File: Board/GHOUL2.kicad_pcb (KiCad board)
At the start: 2 copper layers, 105.4 x 88.9 mm, 29 parts

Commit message: fixed jb's poor job
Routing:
- net SDA: track 81.5 -> 83.0 mm
- net SCL: track 66.0 -> 67.5 mm
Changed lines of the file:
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@@
     (effects (font (size 1 1) (thickness 0.15)))
   )
+  (segment (start 118.063827 71.062) (end 146.259251 71.062) (width 0.25) (layer "F.Cu") (net 1))
+  (segment (start 151.384 76.2) (end 152.720991 76.2) (width 0.25) (layer "F.Cu") (net 1))
+  (segment (start 146.259251 71.062) (end 151.384 76.186749) (width 0.25) (layer "F.Cu") (net 1))
+  (segment (start 151.384 76.186749) (end 151.384 76.2) (width 0.25) (layer "F.Cu") (net 1))
+  (segment (start 152.720991 76.2) (end 153.67 77.149009) (width 0.25) (layer "F.Cu") (net 1))
+  (segment (start 113.941827 75.184) (end 118.063827 71.062) (width 0.25) (layer "F.Cu") (net 1))
+  (segment (start 103.632 73.66) (end 105.156 75.184) (width 0.25) (layer "F.Cu") (net 1))
+  (segment (start 153.67 77.149009) (end 153.67 81.28) (width 0.25) (layer "F.Cu") (net 1))
   (segment (start 153.67 81.28) (end 152.4 82.55) (width 0.25) (layer "F.Cu") (net 1))
-  (segment (start 113.941827 75.184) (end 118.063827 71.062) (width 0.25) (layer "F.Cu") (net 1))
-  (segment (start 153.67 77.149009) (end 153.67 81.28) (width 0.25) (layer "F.Cu") (net 1))
-  (segment (start 151.275 76.077749) (end 152.59874 76.077749) (width 0.25) (layer "F.Cu") (net 1))
-  (segment (start 152.59874 76.077749) (end 153.67 77.149009) (width 0.25) (layer "F.Cu") (net 1))
-  (segment (start 118.063827 71.062) (end 146.259251 71.062) (width 0.25) (layer "F.Cu") (net 1))
-  (segment (start 146.259251 71.062) (end 151.275 76.077749) (width 0.25) (layer "F.Cu") (net 1))
   (segment (start 105.156 75.184) (end 113.941827 75.184) (width 0.25) (layer "F.Cu") (net 1))
-  (segment (start 103.632 73.66) (end 105.156 75.184) (width 0.25) (layer "F.Cu") (net 1))
   (segment (start 187.065 113.03) (end 192.024 113.03) (width 0.25) (layer "F.Cu") (net 2))
   (segment (start 171.965 130.055) (end 185.47 130.055) (width 0.25) (layer "F.Cu") (net 3))
@@
   (segment (start 148.810405 90.075) (end 145.955 90.075) (width 0.25) (layer "F.Cu") (net 22))
   (segment (start 123.952 73.66) (end 140.367 90.075) (width 0.25) (layer "F.Cu") (net 22))
-  (segment (start 152.720991 121.92) (end 131.025 121.92) (width 0.25) (layer "F.Cu") (net 23))
+  (segment (start 152.720991 121.92) (end 131.064 121.92) (width 0.25) (layer "F.Cu") (net 23))
   (segment (start 152.4 125.73) (end 153.525 124.605) (width 0.25) (layer "F.Cu") (net 23))
+  (segment (start 127.349 118.205) (end 127.31 118.205) (width 0.25) (layer "F.Cu") (net 23))
   (segment (start 153.525 122.724009) (end 152.720991 121.92) (width 0.25) (layer "F.Cu") (net 23))
   (segment (start 153.525 124.605) (end 153.525 122.724009) (width 0.25) (layer "F.Cu") (net 23))
-  (segment (start 131.025 121.92) (end 127.31 118.205) (width 0.25) (layer "F.Cu") (net 23))
-  (segment (start 127.31 120.745) (end 129.755 123.19) (width 0.25) (layer "F.Cu") (net 24))
-  (segment (start 129.755 123.19) (end 152.4 123.19) (width 0.25) (layer "F.Cu") (net 24))
-  (segment (start 155.822591 90.17) (end 154.94 90.17) (width 0.25) (layer "F.Cu") (net 25))
+  (segment (start 131.064 121.92) (end 127.349 118.205) (width 0.25) (layer "F.Cu") (net 23))
+  (segment (start 127.31 120.745) (end 128.935 122.37) (width 0.25) (layer "F.Cu") (net 24))
+  (segment (start 128.935 122.37) (end 151.58 122.37) (width 0.25) (layer "F.Cu") (net 24))
+  (segment (start 151.58 122.37) (end 152.4 123.19) (width 0.25) (layer "F.Cu") (net 24))
+  (segment (start 151.035 111.76) (end 145.955 106.68) (width 0.25) (layer "F.Cu") (net 25))
+  (segment (start 167.64 92.71) (end 167.64 93.472) (width 0.25) (layer "F.Cu") (net 25))
+  (segment (start 167.64 92.71) (end 166.82 91.89) (width 0.25) (layer "F.Cu") (net 25))
   (segment (start 147.042 78.462) (end 145.955 77.375) (width 0.25) (layer "F.Cu") (net 25))
-  (segment (start 152.941496 111.76) (end 151.035 111.76) (width 0.25) (layer "F.Cu") (net 25))
-  (segment (start 167.64 92.71) (end 163.83 96.52) (width 0.25) (layer "F.Cu") (net 25))
-  (segment (start 154.94 90.17) (end 153.525 88.755) (width 0.25) (layer "F.Cu") (net 25))
-  (segment (start 153.525 88.755) (end 150.985 88.755) (width 0.25) (layer "F.Cu") (net 25))
-  (segment (start 167.64 92.71) (end 158.362591 92.71) (width 0.25) (layer "F.Cu") (net 25))
-  (segment (start 151.035 111.76) (end 145.955 106.68) (width 0.25) (layer "F.Cu") (net 25))
-  (segment (start 150.985 88.755) (end 147.042 84.812) (width 0.25) (layer "F.Cu") (net 25))
-  (segment (start 158.362591 92.71) (end 155.822591 90.17) (width 0.25) (layer "F.Cu") (net 25))
-  (segment (start 163.83 100.871496) (end 152.941496 111.76) (width 0.25) (layer "F.Cu") (net 25))
-  (segment (start 163.83 96.52) (end 163.83 100.871496) (width 0.25) (layer "F.Cu") (net 25))
   (segment (start 147.042 84.812) (end 147.042 78.462) (width 0.25) (layer "F.Cu") (net 25))
+  (segment (start 163.83 97.282) (end 163.83 103.503604) (width 0.25) (layer "F.Cu") (net 25))
+  (segment (start 166.82 91.89) (end 159.833604 91.89) (width 0.25) (layer "F.Cu") (net 25))
+  (segment (start 159.833604 91.89) (end 156.843604 88.9) (width 0.25) (layer "F.Cu") (net 25))
+  (segment (start 156.843604 88.9) (end 151.13 88.9) (width 0.25) (layer "F.Cu") (net 25))
+  (segment (start 167.64 93.472) (end 163.83 97.282) (width 0.25) (layer "F.Cu") (net 25))
+  (segment (start 155.573604 111.76) (end 151.035 111.76) (width 0.25) (layer "F.Cu") (net 25))
+  (segment (start 151.13 88.9) (end 147.042 84.812) (width 0.25) (layer "F.Cu") (net 25))
+  (segment (start 163.83 103.503604) (end 155.573604 111.76) (width 0.25) (layer "F.Cu") (net 25))
   (segment (start 164.28 98.61) (end 164.28 103.69) (width 0.25) (layer "F.Cu") (net 26))
+  (segment (start 145.955 74.835) (end 147.492 76.372) (width 0.25) (layer "F.Cu") (net 26))
   (segment (start 164.28 103.69) (end 153.67 114.3) (width 0.25) (layer "F.Cu") (net 26))
   (segment (start 150.876 114.3) (end 147.066 110.49) (width 0.25) (layer "F.Cu") (net 26))
-  (segment (start 151.747 86.215) (end 153.525 86.215) (width 0.25) (layer "F.Cu") (net 26))
-  (segment (start 145.955 74.835) (end 147.492 76.372) (width 0.25) (layer "F.Cu") (net 26))
-  (segment (start 156.0142 87.4342) (end 160.02 91.44) (width 0.25) (layer "F.Cu") (net 26))
+  (segment (start 168.91 93.98) (end 167.64 95.25) (width 0.25) (layer "F.Cu") (net 26))
   (segment (start 167.64 95.25) (end 164.28 98.61) (width 0.25) (layer "F.Cu") (net 26))
-  (segment (start 151.275 83.965) (end 151.275 85.743) (width 0.25) (layer "F.Cu") (net 26))
+  (segment (start 147.492 76.372) (end 147.492 84.625604) (width 0.25) (layer "F.Cu") (net 26))
+  (segment (start 149.226396 86.36) (end 154.94 86.36) (width 0.25) (layer "F.Cu") (net 26))
+  (segment (start 153.67 114.3) (end 150.876 114.3) (width 0.25) (layer "F.Cu") (net 26))
+  (segment (start 147.492 84.625604) (end 149.226396 86.36) (width 0.25) (layer "F.Cu") (net 26))
+  (segment (start 144.526 103.029) (end 145.955 101.6) (width 0.25) (layer "F.Cu") (net 26))
+  (segment (start 154.94 86.36) (end 160.02 91.44) (width 0.25) (layer "F.Cu") (net 26))
+  (segment (start 147.066 110.49) (end 145.542 110.49) (width 0.25) (layer "F.Cu") (net 26))
   (segment (start 168.181496 91.44) (end 168.91 92.168504) (width 0.25) (layer "F.Cu") (net 26))
-  (segment (start 147.492 80.182) (end 151.275 83.965) (width 0.25) (layer "F.Cu") (net 26))
-  (segment (start 153.67 114.3) (end 150.876 114.3) (width 0.25) (layer "F.Cu") (net 26))
-  (segment (start 144.526 103.029) (end 145.955 101.6) (width 0.25) (layer "F.Cu") (net 26))
-  (segment (start 151.275 85.743) (end 151.747 86.215) (width 0.25) (layer "F.Cu") (net 26))
-  (segment (start 147.066 110.49) (end 145.542 110.49) (width 0.25) (layer "F.Cu") (net 26))
+  (segment (start 160.02 91.44) (end 168.181496 91.44) (width 0.25) (layer "F.Cu") (net 26))
+  (segment (start 145.542 110.49) (end 144.526 109.474) (width 0.25) (layer "F.Cu") (net 26))
   (segment (start 168.91 92.168504) (end 168.91 93.98) (width 0.25) (layer "F.Cu") (net 26))
-  (segment (start 160.02 91.44) (end 168.181496 91.44) (width 0.25) (layer "F.Cu") (net 26))
-  (segment (start 154.7442 87.4342) (end 156.0142 87.4342) (width 0.25) (layer "F.Cu") (net 26))
-  (segment (start 153.525 86.215) (end 154.7442 87.4342) (width 0.25) (layer "F.Cu") (net 26))
-  (segment (start 168.91 93.98) (end 167.64 95.25) (width 0.25) (layer "F.Cu") (net 26))
-  (segment (start 145.542 110.49) (end 144.526 109.474) (width 0.25) (layer "F.Cu") (net 26))
-  (segment (start 147.492 76.372) (end 147.492 80.182) (width 0.25) (layer "F.Cu") (net 26))
   (segment (start 144.526 109.474) (end 144.526 103.029) (width 0.25) (layer "F.Cu") (net 26))
   (segment (start 149.04 91.89) (end 152.4 95.25) (width 0.25) (layer "F.Cu") (net 28))

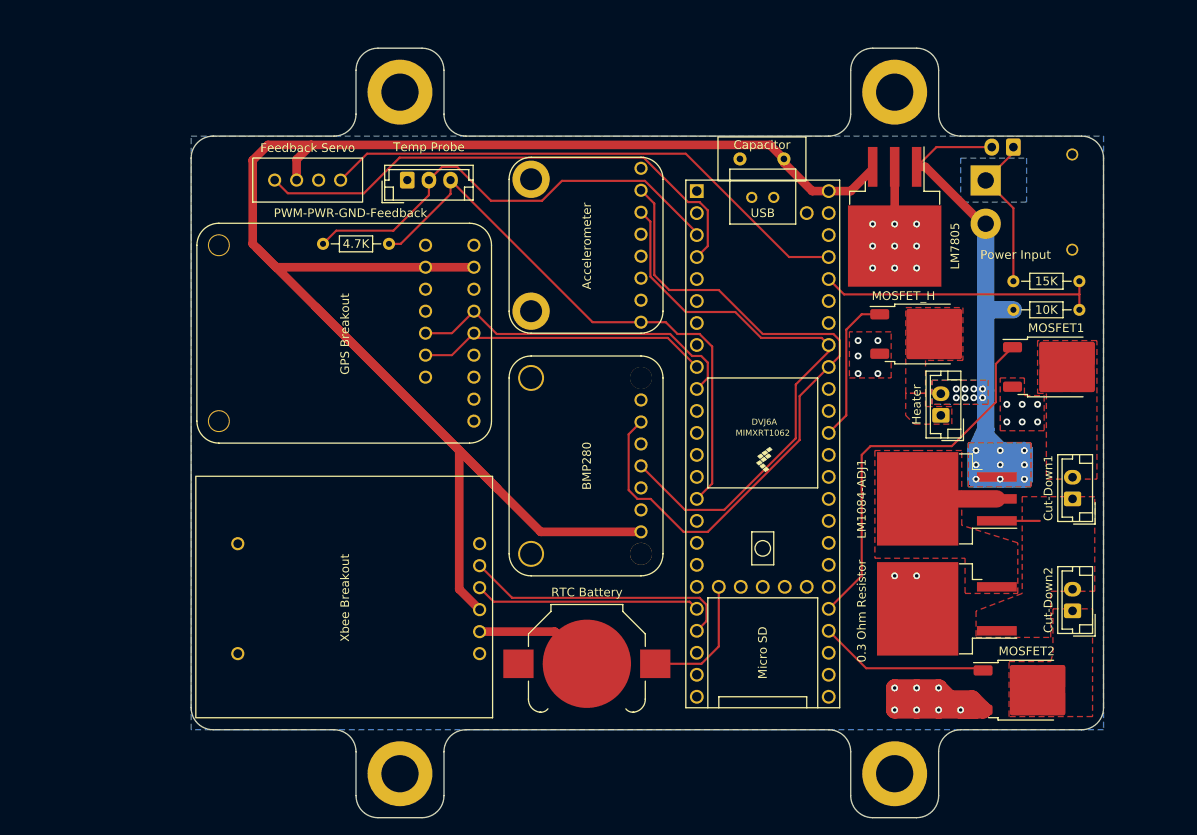
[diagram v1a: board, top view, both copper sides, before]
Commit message: added gps, buck, pressure and clean up
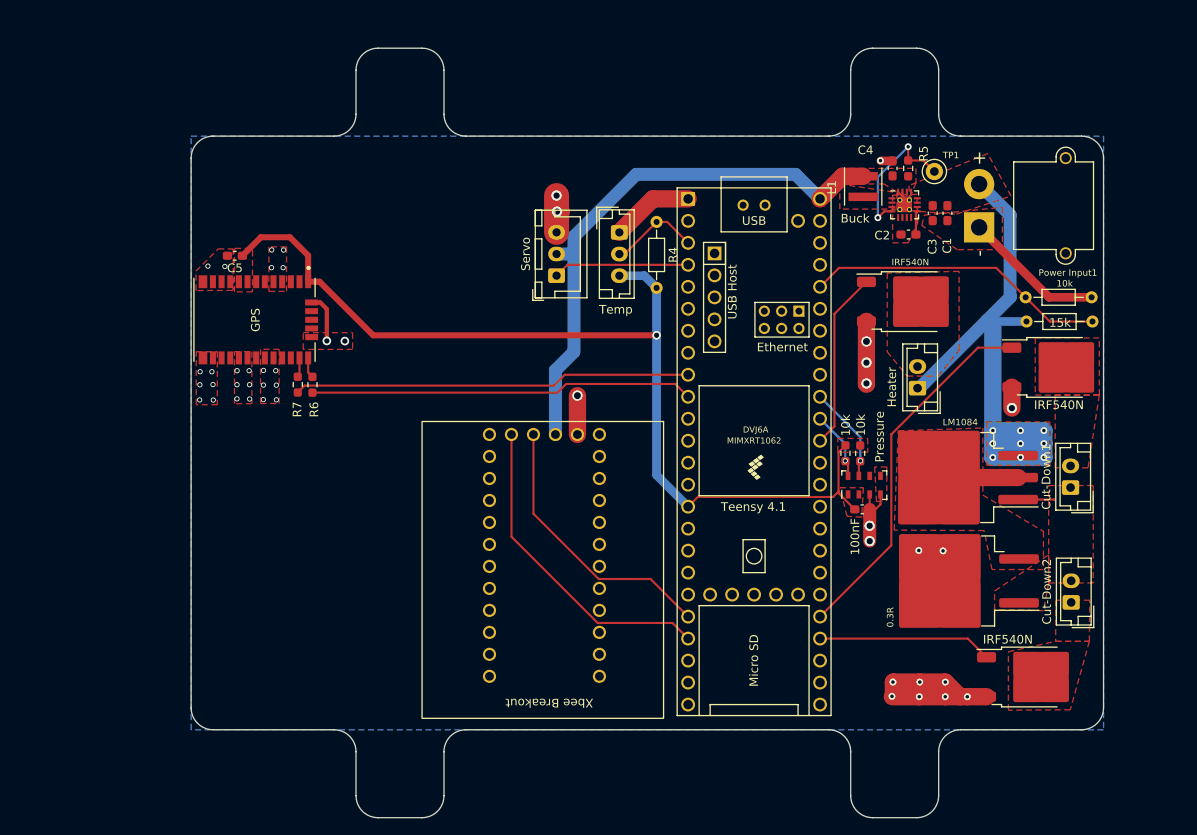
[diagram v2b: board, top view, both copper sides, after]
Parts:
- removed  : Teensy4.1, teensy.pretty-master:Teensy41
- removed 0.3 Ohm Resistor: 03, Package_TO_SOT_SMD:TO-263-2
- removed 10K: 10K, Resistor_THT:R_Axial_DIN0204_L3.6mm_D1.6mm_P7.62mm_Horizontal
- removed 15K: 15K, Resistor_THT:R_Axial_DIN0204_L3.6mm_D1.6mm_P7.62mm_Horizontal
- removed 4.7K: 4.7K, Resistor_THT:R_Axial_DIN0204_L3.6mm_D1.6mm_P7.62mm_Horizontal
- removed ? (x3): , 
- removed Accelerometer: GHOULIMU, GHOULFootPrints:GHOULIMU
- removed BMP280: BMP280, GHOULFootPrints:BMP280
- removed BT1: Battery_Cell, Battery:BatteryHolder_Keystone_3000_1x12mm
- removed Capacitor: C 10 nano-farad, GHOULFootPrints:GhoulResistor
- removed Feedback Servo: Feedback_Serv, GHOULFootPrints:ServoPinout
- removed GPS Breakout: Ultimate_GPS_Breakout_v3, GHOULFootPrints:Ultimate GPS Breakout v3
- removed LM1084-ADJ1: LM1084-ADJ, Package_TO_SOT_SMD:TO-263-3_TabPin2
- removed LM7805: LM7805_TO220, Package_TO_SOT_SMD:TO-263-3_TabPin2
- removed MOSFET1, MOSFET2, MOSFET_H: IRF540N, Package_TO_SOT_SMD:TO-252-2
- removed Power Input: Conn_01x02, Connector_AMASS:AMASS_XT30PW-M_1x02_P2.50mm_Horizontal
- removed REF** (x2), locked: MountingHole_4.3mm_M4_DIN965_Pad, mechanical:MountingHole_4.3mm_M4_DIN965_Pad
- removed Temp Probe: DS18S20, Connector_JST:JST_EH_B3B-EH-A_1x03_P2.50mm_Vertical
- added 0.3R: 03, Package_TO_SOT_SMD:TO-263-2, F.Cu at (182.0, 120.0)
- added 100nF: 100nF, Capacitor_SMD:C_0603_1608Metric_Pad1.08x0.95mm_HandSolder, F.Cu at (171.5, 111.7)
- added 10k: 10k, Resistor_SMD:R_0603_1608Metric_Pad0.98x0.95mm_HandSolder, F.Cu at (171.3, 105.2)
- added 10k: 10k, Resistor_SMD:R_0603_1608Metric_Pad0.98x0.95mm_HandSolder, F.Cu at (169.6, 105.2)
- added 10k: 10K, Resistor_THT:R_Axial_DIN0204_L3.6mm_D1.6mm_P7.62mm_Horizontal, F.Cu at (190.4, 87.2)
- added 15k: 15K, Resistor_THT:R_Axial_DIN0204_L3.6mm_D1.6mm_P7.62mm_Horizontal, F.Cu at (190.5, 90.0)
- added Buck: TPS62133, Package_DFN_QFN:VQFN-16-1EP_3x3mm_P0.5mm_EP1.68x1.68mm_ThermalVias, F.Cu at (176.4, 76.5)
- added C1: 10uF, Capacitor_SMD:C_0603_1608Metric_Pad1.08x0.95mm_HandSolder, F.Cu at (181.4, 77.5)
- added C2: 3.3nF, Capacitor_SMD:C_0603_1608Metric_Pad1.08x0.95mm_HandSolder, F.Cu at (176.9, 79.9)
- added C3: 0.1uF, Capacitor_SMD:C_0603_1608Metric_Pad1.08x0.95mm_HandSolder, F.Cu at (179.7, 77.5)
- added C4: 22uF, Capacitor_SMD:C_0603_1608Metric_Pad1.08x0.95mm_HandSolder, F.Cu at (175.0, 72.3)
- added C5: 4.7uF, Capacitor_SMD:C_0603_1608Metric_Pad1.08x0.95mm_HandSolder, F.Cu at (99.0, 82.4)
- added GPS: CAM-M8Q-0, CAM-M8Q-0:LCC100P960X1400X210-31N, F.Cu at (101.3, 89.8)
- added IRF540N: IRF540N, Package_TO_SOT_SMD:TO-252-2, F.Cu at (193.8, 95.3)
- added IRF540N: IRF540N, Package_TO_SOT_SMD:TO-252-2, F.Cu at (190.9, 131.1)
- added IRF540N: IRF540N, Package_TO_SOT_SMD:TO-252-2, F.Cu at (177.0, 87.7)
- added L1: 1uH, Inductor_SMD:L_Coilcraft_XxL4040, F.Cu at (171.6, 74.4)
- added LM1084: LM1084-ADJ, Package_TO_SOT_SMD:TO-263-3_TabPin2, F.Cu at (181.9, 108.0)
- added Power Input1: Conn_01x02, Connector_AMASS:AMASS_XT30PW-M_1x02_P2.50mm_Horizontal, F.Cu at (185.0, 79.1)
- added Pressure: MS5607-02BA, Package_LGA:LGA-8_3x5mm_P1.25mm, F.Cu at (171.8, 108.9)
- added R4: 4.7K, Resistor_THT:R_Axial_DIN0204_L3.6mm_D1.6mm_P7.62mm_Horizontal, F.Cu at (147.8, 78.5)
- added R5: 100k, Resistor_SMD:R_0603_1608Metric_Pad0.98x0.95mm_HandSolder, F.Cu at (176.8, 72.3)
- added R6: 220, Resistor_SMD:R_0603_1608Metric_Pad0.98x0.95mm_HandSolder, F.Cu at (108.0, 97.3)
- added R7: 220, Resistor_SMD:R_0603_1608Metric_Pad0.98x0.95mm_HandSolder, F.Cu at (106.3, 97.3)
- added Servo: Motor_Servo, Connector_JST:JST_XH_B3B-XH-A_1x03_P2.50mm_Vertical, F.Cu at (136.2, 84.7)
- added TP1: TestPoint, TestPoint:TestPoint_Keystone_5000-5004_Miniature, F.Cu at (179.8, 72.7)
- added Teensy 4.1: Teensy4.1, teensy.pretty-master:Teensy41, F.Cu at (159.0, 105.0)
- added Temp: DS18S20, Connector_JST:JST_EH_B3B-EH-A_1x03_P2.50mm_Vertical, F.Cu at (143.5, 79.7)
- moved Xbee Breakout 39.5 mm to (148.6, 101.5), turned to 180 degrees
- moved Heater 4.14 mm to (177.9, 97.7)
- moved Cut-Down1 1.33 mm to (195.6, 109.2)
- moved Cut-Down2 0.99 mm to (195.7, 122.5)
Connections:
- Cut-Down2 pad 1: Net-(Cut-Down1-In) -> Net-(Cut-Down2-In)
- Cut-Down2 pad 2: Net-(Cut-Down2-Out) -> Net-(Cut-Down1-In)
- Heater pad 1: Net-(MOSFET_H1-D) -> +BATT
- Heater pad 2: Vin -> Net-(MOSFET_H1-D)
- Xbee Breakout pad 2: 5v pwr -> +5V
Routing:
- net 5v pwr: track 224.5 -> 0.00 mm
- net +3.3V: track 0.00 -> 113.5 mm, vias 0 -> 1
- net SDA: track 83.0 -> 0.00 mm
- net Vin: track 78.1 -> 0.00 mm, vias 17 -> 0
- net +BATT: track 0.00 -> 71.5 mm, vias 0 -> 9
- net 3v3 pwr: track 67.9 -> 0.00 mm
- net SCL: track 67.5 -> 0.00 mm
- net +5V: track 0.00 -> 64.5 mm
- net Feedback: track 62.6 -> 0.00 mm
- net Net-(U1-1_TX1_CTX2_MISO1): track 53.2 -> 0.00 mm
- net GPSTx: track 0.00 -> 45.9 mm
- net Servo PWM: track 60.8 -> 15.7 mm
- net GPSRx: track 0.00 -> 44.4 mm
- net Net-(GPS Breakout1-RX): track 39.7 -> 0.00 mm
- net Net-(GPS Breakout1-TX): track 34.0 -> 0.00 mm
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- added copper zone on F.Cu, net +3.3V
- added copper zone on F.Cu, net +5V
- added copper zone on F.Cu, net +BATT
- added copper zone on F.Cu, net Net-(Cut-Down2-In)
- added copper zone on F.Cu, net Net-(L1-Pad1)
- removed copper zone on F.Cu, net Net-(Cut-Down2-Out)
- removed copper zone on B.Cu, net Vin
- removed copper zone on F.Cu, net Vin
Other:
- board text removed: "PWM-PWR-GND-Feedback"
- board text removed: "RTC Battery"

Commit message: changes lol
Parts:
- added REF**: MountingHole_4.3mm_M4_DIN965_Pad, mechanical:MountingHole_4.3mm_M4_DIN965_Pad, F.Cu at (175.3, 63.5)
- added REF**: MountingHole_4.3mm_M4_DIN965_Pad, mechanical:MountingHole_4.3mm_M4_DIN965_Pad, F.Cu at (118.1, 63.5)
- added REF**: MountingHole_4.3mm_M4_DIN965_Pad, mechanical:MountingHole_4.3mm_M4_DIN965_Pad, F.Cu at (118.1, 142.2)
- added REF**: MountingHole_4.3mm_M4_DIN965_Pad, mechanical:MountingHole_4.3mm_M4_DIN965_Pad, F.Cu at (175.3, 142.2)
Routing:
- net Net-(U3-RF_IN): track 0.00 -> 22.2 mm

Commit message: shipman fix it
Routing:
- net GND: track 86.9 -> 63.1 mm, vias 45 -> 67

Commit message: mostly fixed
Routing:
- net Net-(U3-RF_IN): track 22.2 -> 0.00 mm
- net Baro_SDA: track 11.2 -> 12.9 mm
- net +3.3V: track 113.5 -> 114.7 mm
- net Baro_SCL: track 8.00 -> 9.17 mm
- net GND: vias 67 -> 32
- added copper zone on F.Cu, net Net-(U3-RF_IN)
